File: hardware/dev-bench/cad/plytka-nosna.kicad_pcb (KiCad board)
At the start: 2 copper layers, 170 x 100 mm, 65 parts, among them J1 ARDUINO POWER, J10 CC1120EM P2, J11 ANALIZATOR, J12 VTEST 0-15V, J2 ARDUINO A0-A5, J3 ARDUINO D0-D7, J4 ARDUINO D8-SCL, J5 DEVKITC J1, J6 DEVKITC J3, J7 SHARP 4694, J8 FRAM 4719, J9 CC1120EM P1, Q1 MMBT3904, SW1 GÓRA, SW2 DÓŁ, SW3 OK, SW4 WSTECZ, SW5 CISZA, SW6 PRZYGOTOWANIE

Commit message: Dev bench: carrier N1 after the review against manufacturers' documents (F83)
- J7: Adafruit 4694 pin order VIN..EIN with the display face up; the old
  order followed the parts-side fab print and shorted +3V3 to GND.
- JP3 moved next to J11, outside the X-NUCLEO-S2868A2 outline.
- J9/J10: Samtec TFM-110-01-L-D through-hole, the listed SFM mate
  (FTS-...-DV was an SMT part).
- Pin names on the silkscreen at J7 and J8, P20 band on the 1:1 print,
  solid GND pad J7.3.
- Fabrication package for a quote: FAB-NOTES.txt (also in the ZIP),
  English assembly BOM and SMD placement list.
- Board rerouted (Freerouting 2.5.0 needs Java 25), ERC 0, DRC 0,
  reproduction checked; pre-order list, bring-up and docs updated.

Co-Authored-By: Claude Opus 5.5 <noreply@anthropic.com>
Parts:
- moved JP3 26.4 mm to (161.0, 118.0)
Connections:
- J7 pad 1: /LCD_EXTCOMIN -> /+5V
- J7 pad 2: /LCD_DISP -> unconnected-(J7-Pin_2-Pad2)
- J7 pad 3: /+3V3 -> /GND
- J7 pad 4: /LCD_CS -> /SPI_SCK
- J7 pad 6: /SPI_SCK -> /LCD_CS
- J7 pad 7: /GND -> /+3V3
- J7 pad 8: unconnected-(J7-Pin_8-Pad8) -> /LCD_DISP
- J7 pad 9: /+5V -> /LCD_EXTCOMIN
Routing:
- net /LCD_DISP: track 182.6 -> 222.5 mm, vias 1 -> 2
- net /SPI_SCK: track 294.1 -> 258.3 mm, vias 5 -> 3
- net /SPI_MOSI: track 277.9 -> 249.1 mm
- net /LCD_CS: track 217.9 -> 244.3 mm, vias 1 -> 4
- net /RF_GPIO2: track 170.9 -> 148.0 mm, vias 0 -> 2
- net /+3V3: track 376.1 -> 393.7 mm
- net /SPI_MISO: track 176.5 -> 192.3 mm, vias 4 -> 0
- net /LED_ALARM: track 137.4 -> 152.8 mm, vias 2 -> 3
- net /BTN_OK: track 137.7 -> 124.4 mm
- net /BTN_PREP: track 140.3 -> 152.3 mm, vias 0 -> 1
- net /GND: track 520.4 -> 531.7 mm, vias 7 -> 5
- net /BTN_DOWN: track 173.1 -> 182.7 mm
- net /SW_CISZA: track 154.6 -> 162.8 mm, vias 5 -> 3
- net /+5V_DEVKIT: track 7.69 -> 12.5 mm
- net /BTN_UP: track 197.5 -> 192.7 mm, vias 1 -> 0
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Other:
- board text added: "3V3"
- board text added: "CLK"
- board text added: "CS"
- board text added: "DI"
- board text added: "DISP"
- board text added: "EIN"
- board text added: "EMD"
- board text added: "HOLD"
- board text added: "MISO"
- board text added: "MOSI"
- board text added: "SCK"
- board text added: "Sharp 4694 ekranem do góry"
- board text added: "VIN"
- board text added: "WP"
- board text added: "pas bez miedzi nad P20 płytki DK"
- board text removed: "Sharp 4694"

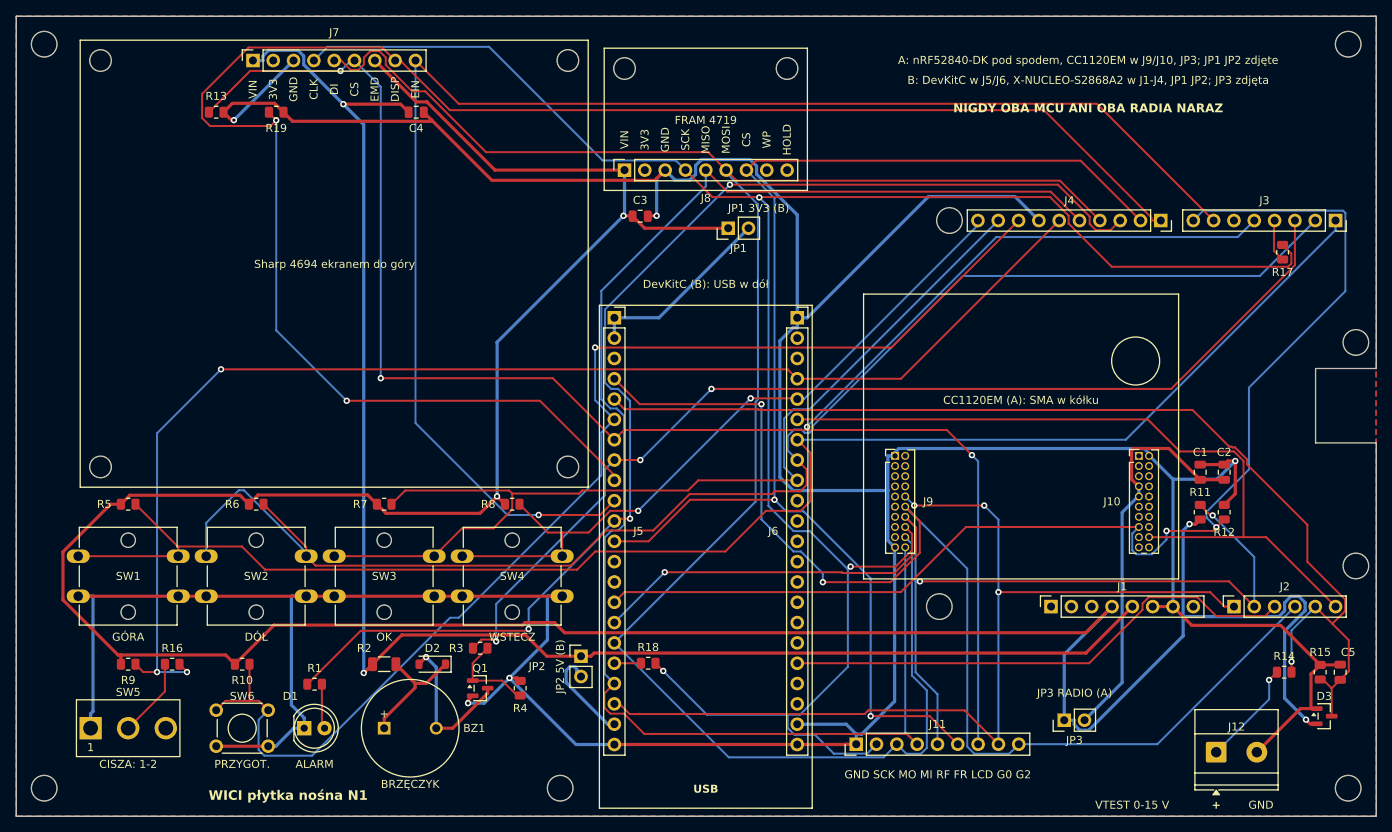
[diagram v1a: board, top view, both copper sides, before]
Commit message: Dev bench N1: fabrication package after fab and assembler review
Fab and assembly house view of the N1 package: paste layer in the
Gerbers, 10 uF capacitor as CL21A106KAYNNNE (taped), HAL lead-free
finish in job.gbrjob, copper 0.3 mm from holes (DRC rule), silk lines
0.15 mm, assembler BOM with SMD parts only, title block on montaz.pdf,
FAB-NOTES with the stated tolerances and assembly scope.

Docs after the final orientation check: P20 band is copper-free on
B.Cu with no vias, P5 notch margin about 0.55 mm on the J11 side,
full list of parts under the X-NUCLEO, DK J2 USB plug under J6 in the
fit check, TFM mated height with SFM-02 to be measured.

Board regenerated with the kept routing session; ERC 0, DRC 0.

Co-Authored-By: Claude Opus 5.5 <noreply@anthropic.com>
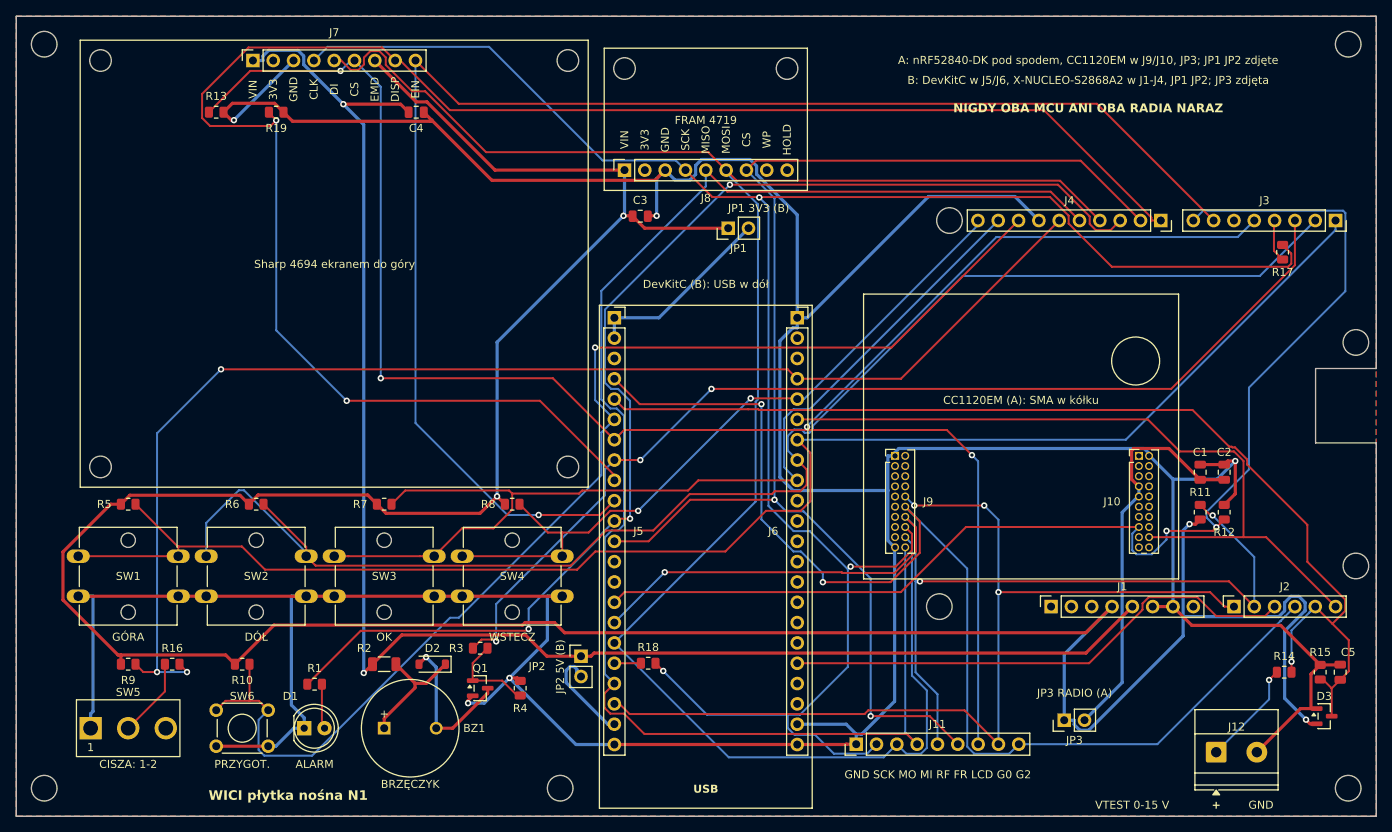
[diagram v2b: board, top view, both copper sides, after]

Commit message: Dev bench N1: production FRAM and Sharp panel on the board (F86)
The Adafruit 4719 FRAM board is out of stock until 2027 and both Adafruit
boards come from a single vendor, so the bench could not be built and did
not exercise the parts the station will use. N1 now carries them directly:

- FRAM U1 in SOIC-8: Infineon CY15B104QN-50SXI or RAMXEED MB85RS4MTPF,
  with 10 kOhm CS pull-up; WP and HOLD/RESET tied to 3.3 V.
- Sharp LS027B7DH01A panel on 0.8 mm foam tape over the board, in a
  Hirose FH12-10S-0.5SH FPC connector (J7) powered from the 5 V rail,
  with the capacitors the Sharp datasheet recommends; generator asserts
  nothing sits under the panel.
- Samtec SSQ stacking sockets for J1-J4 instead of the Adafruit 85 kit.
- Firmware recognises CY15B104QN (C2 2C) and rejects 1.8 V variants.

Rerouted (Freerouting 2.5.0, 0 unrouted), ERC/DRC 0, reproduction
identical. Docs, BOM, cost and bring-up updated; open: panel supply on
bench B (DevKitC 5V pin 4.6-4.8 V vs 4.8 V minimum), J7 position at fit
check.

Co-Authored-By: Claude Opus 5.5 <noreply@anthropic.com>
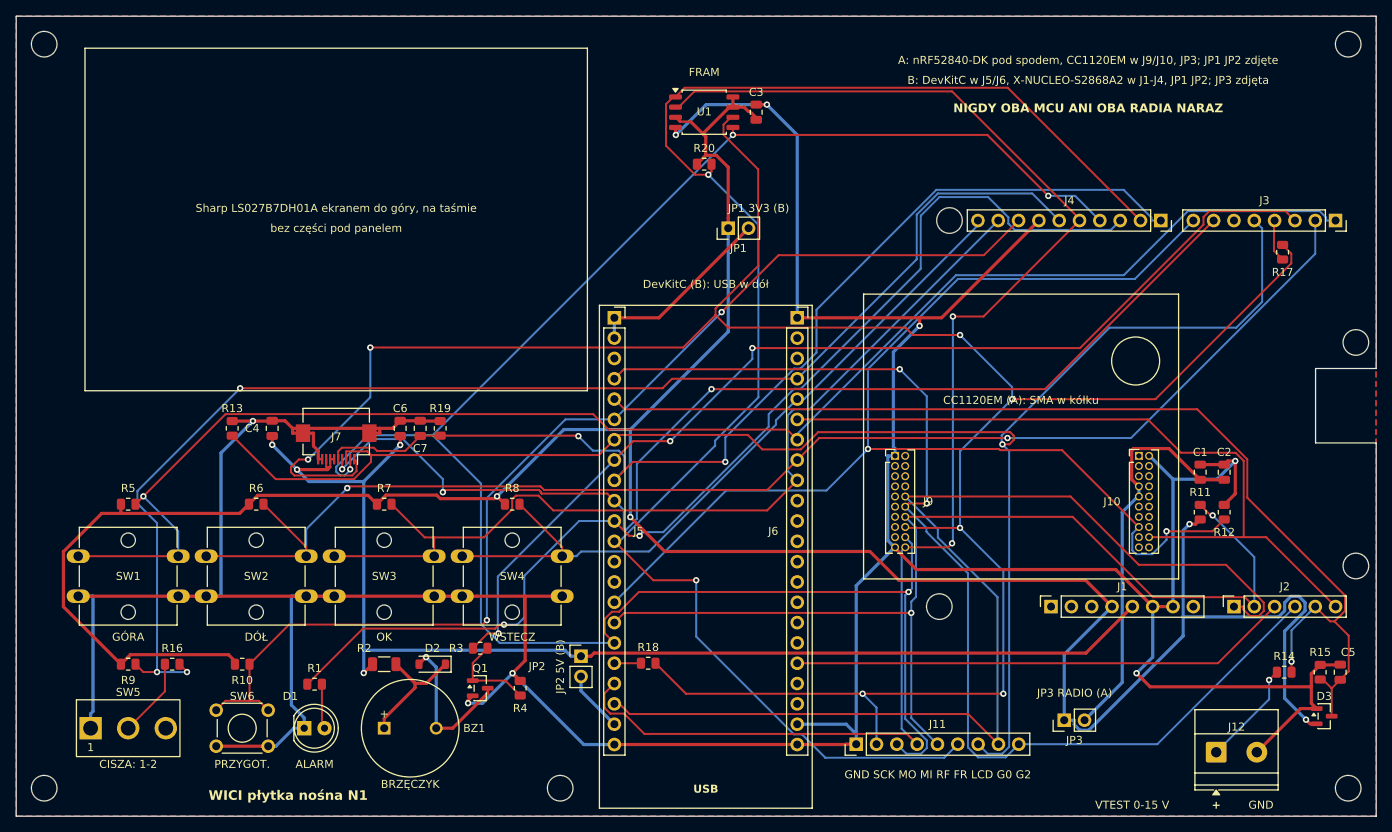
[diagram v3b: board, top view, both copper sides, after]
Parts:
- removed H10, H11, H12, H13, H14, H15: M2.5, MountingHole:MountingHole_2.7mm_M2.5
- removed J8: FRAM 4719, Connector_PinSocket_2.54mm:PinSocket_1x09_P2.54mm_Vertical
- added C6: 100n, Capacitor_SMD:C_0805_2012Metric, F.Cu at (78.0, 81.5)
- added C7: 100n, Capacitor_SMD:C_0805_2012Metric, F.Cu at (80.5, 81.5)
- added R20: 10k, Resistor_SMD:R_0805_2012Metric, F.Cu at (116.0, 48.5)
- added U1: CY15B104QN-50SXI, Package_SO:SOIC-8_5.3x5.3mm_P1.27mm, F.Cu at (116.0, 42.0)
- J7: value SHARP 4694 -> SHARP LS027B7DH01A; footprint Connector_PinSocket_2.54mm:PinSocket_1x09_P2.54mm_Vertical -> Connector_FFC-FPC:Hirose_FH12-10S-0.5SH_1x10-1MP_P0.50mm_Horizontal
- R19: value 2k2 -> 10k
- moved J7 49.1 mm to (70.0, 83.5), turned to 180 degrees
- moved R19 44.5 mm to (83.0, 81.5), turned to 90 degrees
- moved C4 43.4 mm to (62.0, 81.5), turned to 90 degrees
- moved R13 39.6 mm to (57.0, 81.5), turned to 90 degrees
- moved C3 19.5 mm to (122.5, 42.0), turned to 90 degrees
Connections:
- J7 pad 1: /+5V -> /SPI_SCK
- J7 pad 2: unconnected-(J7-Pin_2-Pad2) -> /SPI_MOSI
- J7 pad 3: /GND -> /LCD_CS
- J7 pad 4: /SPI_SCK -> /LCD_EXTCOMIN
- J7 pad 5: /SPI_MOSI -> /LCD_DISP
- J7 pad 6: /LCD_CS -> /+5V
- J7 pad 7: /+3V3 -> /+5V
- J7 pad 8: /LCD_DISP -> /+5V
- J7 pad 9: /LCD_EXTCOMIN -> /GND
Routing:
- net /LCD_DISP: track 222.5 -> 132.6 mm
- net /+3V3: track 393.7 -> 338.1 mm
- net /LCD_EXTCOMIN: track 183.7 -> 139.2 mm, vias 1 -> 3
- net /+5V: track 198.0 -> 153.7 mm, vias 2 -> 4
- net /LCD_CS: track 244.3 -> 205.1 mm, vias 4 -> 1
- net /SPI_SCK: track 258.3 -> 292.5 mm, vias 3 -> 7
- net /FRAM_CS: track 163.3 -> 195.7 mm
- net /GND: track 531.7 -> 510.0 mm, vias 5 -> 8
- net /RF_GPIO0: track 121.6 -> 141.9 mm, vias 3 -> 0
- net /LED_ALARM: track 152.8 -> 138.9 mm, vias 3 -> 2
- net /BTN_DOWN: track 182.7 -> 169.5 mm, vias 0 -> 2
- net /BTN_PREP: track 152.3 -> 140.1 mm, vias 1 -> 2
- net /SPI_MISO: track 192.3 -> 183.5 mm, vias 0 -> 2
- net /RF_GPIO2: track 148.0 -> 139.8 mm
- net /SPI_MOSI: track 249.1 -> 241.5 mm, vias 0 -> 4
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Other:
- board text added: "FRAM"
- board text added: "Sharp LS027B7DH01A ekranem do góry, na taśmie"
- board text added: "bez części pod panelem"
- board text removed: "3V3"
- board text removed: "CLK"
- board text removed: "CS"
- board text removed: "DI"
- board text removed: "DISP"
- board text removed: "EIN"
- board text removed: "EMD"
- board text removed: "FRAM 4719"
- board text removed: "HOLD"
- board text removed: "MISO"
- board text removed: "MOSI"
- board text removed: "SCK"
- board text removed: "Sharp 4694 ekranem do góry"
- board text removed: "VIN"
- board text removed: "WP"

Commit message: Dev bench N1: panel boost, EXTCOMIN failure handling, audit fixes (F103)
Update the N1 carrier to the current specification and the N1 audit:
- panel VDD/VDDA from an MCP1640 boost (+5V_LCD, 4.90-5.36 V worst
  case) on both benches; Adafruit 4694 rejected as unavailable
- firmware keeps DISP low and reports a fault when the EXTCOMIN timer
  fails (no software VCOM with EXTMODE=H); FRAM SPI at 8 MHz
- VTEST divider from 0.1% resistors with two-point calibration;
  oscilloscope procedure for J7, radio and FRAM; J7 continuity by pin
  group; ammeter drop check while transmitting
- DRC rules file was silently ignored by kicad-cli; fixed syntax and
  added a canary rule; export refuses to run unless ERC/DRC are clean
- board comparison covers zone fills, fields and attributes
- panel datasheet LCP-1112041; part availability checked 2026-10-08
  (10 uF caps to CL21A106KAYNNNG, DevKitC N8R8 only)

Co-Authored-By: Claude Opus 5.5 <noreply@anthropic.com>
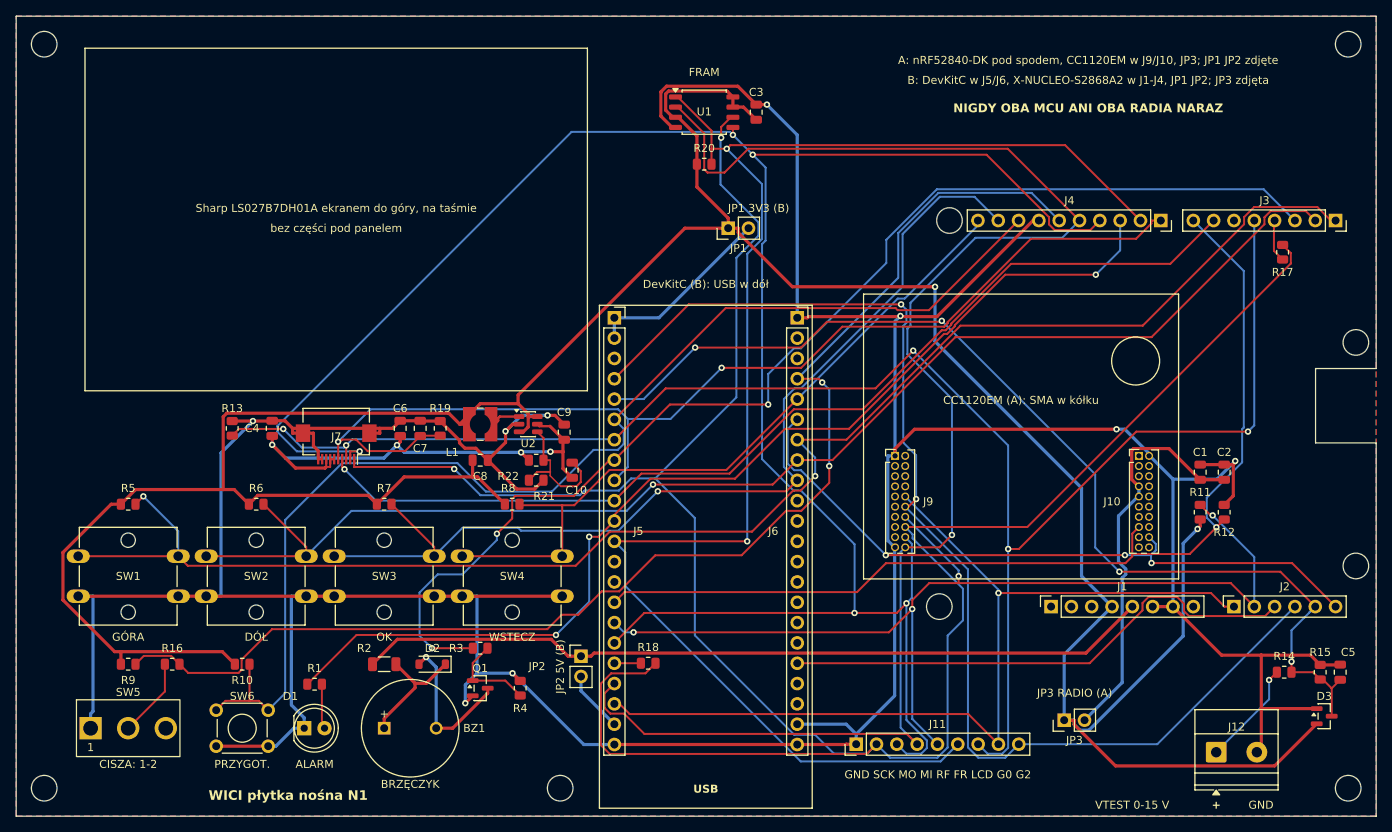
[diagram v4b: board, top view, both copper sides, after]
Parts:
- added C10: 100p, Capacitor_SMD:C_0805_2012Metric, F.Cu at (99.5, 86.8)
- added C8: 10u, Capacitor_SMD:C_0805_2012Metric, F.Cu at (88.0, 85.5)
- added C9: 10u, Capacitor_SMD:C_0805_2012Metric, F.Cu at (98.5, 82.0)
- added L1: 4u7, Inductor_SMD:L_Wuerth_WE-TPC-3816, F.Cu at (88.0, 81.0)
- added R21: 1M, Resistor_SMD:R_0805_2012Metric, F.Cu at (95.0, 85.5)
- added R22: 309k, Resistor_SMD:R_0805_2012Metric, F.Cu at (95.0, 88.0)
- added U2: MCP1640, Package_TO_SOT_SMD:SOT-23-6, F.Cu at (94.0, 81.0)
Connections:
- C4 pad 1: /+5V -> /+5V_LCD
- C6 pad 1: /+5V -> /+5V_LCD
- J7 pad 6: /+5V -> /+5V_LCD
- J7 pad 7: /+5V -> /+5V_LCD
- J7 pad 8: /+5V -> /+5V_LCD
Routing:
- net /+5V_LCD: track 0.00 -> 62.3 mm, vias 0 -> 4
- net /+5V: track 153.7 -> 99.7 mm, vias 4 -> 0
- net /+3V3: track 338.1 -> 389.6 mm, vias 4 -> 2
- net /SPI_MOSI: track 241.5 -> 273.9 mm, vias 4 -> 5
- net /GND: track 510.0 -> 541.6 mm, vias 8 -> 9
- net /RF_GPIO0: track 141.9 -> 116.0 mm, vias 0 -> 1
- net /RF_RESET: track 153.3 -> 127.8 mm, vias 2 -> 1
- net /BUZZER: track 131.5 -> 150.5 mm
- net /BST_FB: track 0.00 -> 17.2 mm
- net /LCD_EXTCOMIN: track 139.2 -> 126.2 mm, vias 3 -> 1
- net /SPI_MISO: track 183.5 -> 195.0 mm, vias 2 -> 1
- net /BTN_PREP: track 140.1 -> 150.5 mm, vias 2 -> 0
- net /LCD_CS: track 205.1 -> 215.1 mm, vias 1 -> 5
- net /RF_GPIO2: track 139.8 -> 149.5 mm
- net /SPI_SCK: track 292.5 -> 302.2 mm, vias 7 -> 2
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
